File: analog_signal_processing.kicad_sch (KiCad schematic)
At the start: 62 parts, among them U3 PT2399, U4 CD4066BE, U5 PT2399, U8 TL072, U9 TL072

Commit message: wip on esp conns
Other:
- moved on the sheet: C34, C35, R26, R29, U4C
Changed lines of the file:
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@@
 	(wire
 		(pts
+			(xy 63.5 172.72) (xy 63.5 165.1)
+		)
+		(stroke
+			(width 0)
+			(type default)
+		)
+	)
+	(wire
+		(pts
 			(xy 243.84 35.56) (xy 247.65 35.56)
 		)
@@
 	(wire
 		(pts
+			(xy 60.96 135.89) (xy 90.17 135.89)
+		)
+		(stroke
+			(width 0)
+			(type default)
+		)
+	)
+	(wire
+		(pts
 			(xy 198.12 54.61) (xy 198.12 55.88)
 		)
@@
 	(wire
 		(pts
-			(xy 67.31 128.27) (xy 67.31 130.81)
+			(xy 38.1 128.27) (xy 38.1 130.81)
 		)
 		(stroke
@@
 	(wire
 		(pts
-			(xy 95.25 146.05) (xy 95.25 147.32)
+			(xy 48.26 172.72) (xy 63.5 172.72)
 		)
 		(stroke
@@
 	(wire
 		(pts
-			(xy 198.12 16.51) (xy 198.12 19.05)
+			(xy 95.25 146.05) (xy 95.25 147.32)
 		)
 		(stroke
@@
 	(wire
 		(pts
-			(xy 138.43 83.82) (xy 138.43 85.09)
+			(xy 198.12 16.51) (xy 198.12 19.05)
 		)
 		(stroke
@@
 	(wire
 		(pts
-			(xy 154.94 31.75) (xy 160.02 31.75)
+			(xy 138.43 83.82) (xy 138.43 85.09)
 		)
 		(stroke
@@
 	(wire
 		(pts
-			(xy 107.95 33.02) (xy 107.95 41.91)
+			(xy 154.94 31.75) (xy 160.02 31.75)
 		)
 		(stroke
@@
 	(wire
 		(pts
-			(xy 63.5 165.1) (xy 63.5 172.72)
+			(xy 107.95 33.02) (xy 107.95 41.91)
 		)
 		(stroke
@@
 	(global_label "AUDIO_IN"
 		(shape input)
-		(at 59.69 135.89 180)
+		(at 30.48 135.89 180)
 		(fields_autoplaced yes)
 		(effects
@@
 		)
 		(property "Intersheetrefs" "${INTERSHEET_REFS}"
-			(at 48.1775 135.89 0)
+			(at 18.9675 135.89 0)
 			(effects
 				(font
@@
 	(global_label "U4C"
 		(shape input)
-		(at 67.31 128.27 0)
+		(at 38.1 128.27 0)
 		(fields_autoplaced yes)
 		(effects
@@
 		)
 		(property "Intersheetrefs" "${INTERSHEET_REFS}"
-			(at 74.1052 128.27 0)
+			(at 44.8952 128.27 0)
 			(effects
 				(font
@@
 	(global_label "Output_Tap"
 		(shape input)
-		(at 48.26 172.72 180)
+		(at 33.02 172.72 180)
 		(fields_autoplaced yes)
 		(effects
@@
 		)
 		(property "Intersheetrefs" "${INTERSHEET_REFS}"
-			(at 34.8127 172.72 0)
+			(at 19.5727 172.72 0)
 			(effects
 				(font
@@
 	(symbol
 		(lib_id "PCM_4ms_Resistor:4.7k_0603")
-		(at 86.36 135.89 90)
+		(at 57.15 135.89 90)
 		(unit 1)
 		(exclude_from_sim no)
@@
 		(dnp no)
 		(property "Reference" "R29"
-			(at 86.36 131.826 90)
+			(at 57.15 131.826 90)
 			(effects
 				(font
@@
 		)
 		(property "Value" "4.7k_0603"
-			(at 86.36 138.43 90)
+			(at 57.15 138.43 90)
 			(effects
 				(font
@@
 		)
 		(property "Footprint" "4ms_Resistor:R_0603"
-			(at 99.06 138.43 0)
+			(at 69.85 138.43 0)
 			(effects
 				(font
@@
 		)
 		(property "Datasheet" ""
-			(at 86.36 135.89 0)
+			(at 57.15 135.89 0)
 			(effects
 				(font
@@
 		)
 		(property "Description" "4k7, 1%, 1/10W, 0603"
-			(at 86.36 135.89 0)
+			(at 57.15 135.89 0)
 			(effects
 				(font
@@
 		)
 		(property "Specifications" "4k7, 1%, 1/10W, 0603"
-			(at 94.234 138.43 0)
+			(at 65.024 138.43 0)
 			(effects
 				(font
@@
 		)
 		(property "Manufacturer" "Yageo"
-			(at 95.758 138.43 0)
+			(at 66.548 138.43 0)
 			(effects
 				(font
@@
 		)
 		(property "Part Number" "RC0603FR-074K7L"
-			(at 97.282 138.43 0)
+			(at 68.072 138.43 0)
 			(effects
 				(font
@@
 		)
 		(property "Display" "4.7k"
-			(at 86.36 133.604 90)
+			(at 57.15 133.604 90)
 			(effects
 				(font
@@
 		)
 		(property "JLCPCB ID" "C23162"
-			(at 86.36 135.89 0)
+			(at 57.15 135.89 0)
 			(effects
 				(font
@@
 	(symbol
 		(lib_id "Device:C_Polarized")
-		(at 59.69 172.72 90)
+		(at 44.45 172.72 90)
 		(unit 1)
 		(exclude_from_sim no)
@@
 		(dnp no)
 		(property "Reference" "C35"
-			(at 59.69 166.878 90)
+			(at 44.45 166.878 90)
 			(effects
 				(font
@@
 		)
 		(property "Value" "47 uF"
-			(at 59.69 168.656 90)
+			(at 44.45 168.656 90)
 			(effects
 				(font
@@
 		)
 		(property "Footprint" ""
-			(at 63.5 171.7548 0)
+			(at 48.26 171.7548 0)
 			(effects
 				(font
@@
 		)
 		(property "Datasheet" "~"
-			(at 59.69 172.72 0)
+			(at 44.45 172.72 0)
 			(effects
 				(font
@@
 		)
 		(property "Description" "Polarized capacitor"
-			(at 59.69 172.72 0)
+			(at 44.45 172.72 0)
 			(effects
 				(font
@@
 		(on_board yes)
 		(dnp no)
-		(fields_autoplaced yes)
 		(property "Reference" "POT2"
-			(at 68.58 167.6399 0)
+			(at 69.342 167.64 0)
 			(effects
 				(font
@@
 		)
 		(property "Display" "10k"
-			(at 68.58 170.1799 0)
+			(at 69.342 170.18 0)
 			(effects
 				(font
@@
 	(symbol
 		(lib_id "PCM_4ms_Resistor:4.7k_0603")
-		(at 52.07 172.72 90)
+		(at 36.83 172.72 90)
 		(unit 1)
 		(exclude_from_sim no)
@@
 		(dnp no)
 		(property "Reference" "R26"
-			(at 52.07 168.656 90)
+			(at 36.83 168.656 90)
 			(effects
 				(font
@@
 		)
 		(property "Value" "4.7k_0603"
-			(at 52.07 175.26 90)
+			(at 36.83 175.26 90)
 			(effects
 				(font
@@
 		)
 		(property "Footprint" "4ms_Resistor:R_0603"
-			(at 64.77 175.26 0)
+			(at 49.53 175.26 0)
 			(effects
 				(font
@@
 		)
 		(property "Datasheet" ""
-			(at 52.07 172.72 0)
+			(at 36.83 172.72 0)
 			(effects
 				(font
@@
 		)
 		(property "Description" "4k7, 1%, 1/10W, 0603"
-			(at 52.07 172.72 0)
+			(at 36.83 172.72 0)
 			(effects
 				(font
@@
 		)
 		(property "Specifications" "4k7, 1%, 1/10W, 0603"
-			(at 59.944 175.26 0)
+			(at 44.704 175.26 0)
 			(effects
 				(font
@@
 		)
 		(property "Manufacturer" "Yageo"
-			(at 61.468 175.26 0)
+			(at 46.228 175.26 0)
 			(effects
 				(font
@@
 		)
 		(property "Part Number" "RC0603FR-074K7L"
-			(at 62.992 175.26 0)
+			(at 47.752 175.26 0)
 			(effects
 				(font
@@
 		)
 		(property "Display" "4.7k"
-			(at 52.07 170.434 90)
+			(at 36.83 170.434 90)
 			(effects
 				(font
@@
 		)
 		(property "JLCPCB ID" "C23162"
-			(at 52.07 172.72 0)
+			(at 36.83 172.72 0)
 			(effects
 				(font
@@
 	(symbol
 		(lib_id "Analog_Switch:CD4066BE")
-		(at 67.31 135.89 180)
+		(at 38.1 135.89 180)
 		(unit 3)
 		(exclude_from_sim no)
@@
 		(fields_autoplaced yes)
 		(property "Reference" "U4"
-			(at 67.31 140.97 0)
+			(at 38.1 140.97 0)
 			(effects
 				(font
@@
 		)
 		(property "Value" "CD4066BE"
-			(at 67.31 143.51 0)
+			(at 38.1 143.51 0)
 			(effects
 				(font
@@
 		)
 		(property "Footprint" "Package_DIP:DIP-14_W7.62mm"
-			(at 67.31 133.35 0)
+			(at 38.1 133.35 0)
 			(effects
 				(font
@@
 		)
 		(property "Datasheet" "https://www.ti.com/lit/ds/symlink/cd4066b.pdf"
-			(at 67.31 135.89 0)
+			(at 38.1 135.89 0)
 			(effects
 				(font
@@
 		)
 		(property "Description" "Quad 20V analog SPST 1:1 switch, DIP-14"
-			(at 67.31 135.89 0)
+			(at 38.1 135.89 0)
 			(effects
 				(font
@@
 	(symbol
 		(lib_id "Device:C_Polarized")
-		(at 78.74 135.89 90)
+		(at 49.53 135.89 90)
 		(unit 1)
 		(exclude_from_sim no)
@@
 		(dnp no)
 		(property "Reference" "C34"
-			(at 78.74 130.048 90)
+			(at 49.53 130.048 90)
 			(effects
 				(font
@@
 		)
 		(property "Value" "47 uF"
-			(at 78.74 131.826 90)
+			(at 49.53 131.826 90)
 			(effects
 				(font
@@
 		)
 		(property "Footprint" ""
-			(at 82.55 134.9248 0)
+			(at 53.34 134.9248 0)
 			(effects
 				(font
@@
 		)
 		(property "Datasheet" "~"
-			(at 78.74 135.89 0)
+			(at 49.53 135.89 0)
 			(effects
 				(font
@@
 		)
 		(property "Description" "Polarized capacitor"
-			(at 78.74 135.89 0)
+			(at 49.53 135.89 0)
 			(effects
 				(font

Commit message: fixed a lot of things
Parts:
- removed C10, C11, C18, C19, C23, C34, C35, C36, C37, C39, C4, C5, C6: 47 uF, symbol Device:C_Polarized
- removed C12, C22, C24, C9: 3.3nF, symbol Device:C
- removed C13, C20, C25, C7: 6.8 nF, symbol Device:C
- removed C14, C15, C16, C17, C21, C26, C27, C28, C29, C8: 100nF, symbol Device:C
- removed C2, C33, C38: 100nF_0603_16V, 4ms_Capacitor:C_0603, symbol PCM_4ms_Capacitor:100nF_0603_16V
- removed R1: 1M, symbol Device:R
- removed R10, R11, R12, R13, R14, R15, R16, R17, R18, R19, R26, R27, R28, R29, R30, R7, R8, R9: 4.7k_0603, 4ms_Resistor:R_0603, symbol PCM_4ms_Resistor:4.7k_0603
- removed R6: 5k, symbol Device:R
- removed U8: TL072, 4ms_Package_SSOP:TSSOP-8_4.4x3mm_Pitch0.65mm, symbol PCM_4ms_IC:TL072
- removed unit 1 of U9
- added AUX_OUT1: NJ2FD-V, Connector_Audio:Jack_6.35mm_Neutrik_NJ2FD-V_Vertical, symbol Connector_Audio:NJ2FD-V
- added C10, C11, C18, C19, C2, C23, C31, C32, C34, C36, C41, C5, C6: 47uF, CAPPRD200W50D525H1250, symbol SamacSys_Parts:REA470M1CBK-0511P
- added C12, C14, C15, C16, C17, C21, C26, C27, C28, C3, C30, C37, C8: 100nF, SR211C104KARTR1, symbol SamacSys_Parts:SR211C104KARTR1
- added C13, C25, C38, C7: 6.8nF, SR211C682MARTR1, symbol SamacSys_Parts:SR211C682MARTR1
- added C20, C22, C24, C9: 3.3nF, RCER72A332K0DBH03A, symbol SamacSys_Parts:RCER72A332K0DBH03A
- added IC1: TL072CP, DIP794W53P254L959H508Q8N, symbol SamacSys_Parts:TL072CP
- added R1: 5k, RESAD1550W60L630D230, symbol SamacSys_Parts:YR1B4K99CC
- added R10, R11, R12, R13, R14, R15, R16, R17, R18, R19, R22, R23, R24, R25, R26, R7, R8, R9: 4.7k, RESAD1590W60L630D240, symbol SamacSys_Parts:MFR-25FRF52-4K7
- added R27: 1M, RESAD1590W60L630D240, symbol SamacSys_Parts:MFR-25FRF52-1M
- added U2: TL072, 4ms_Package_SSOP:TSSOP-8_4.4x3mm_Pitch0.65mm, symbol PCM_4ms_IC:TL072
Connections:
- net +5V: now also C12.1, C28.2, C30.2, U2.5 (+)
- net +9V: now also C37.1, U2.8 (V+)
- net AUDIO_IN: now also R22.1, U2.1, U2.2 (-)
- net EFFECT_OUT: now also AUX_OUT1.T, C23.2
- net MIDDLE_TAP: now also C6.2
- net OUTPUT_TAP: now also C20.1, R16.1
- net Output_Tap: now also C41.2, R24.1
- net at U3.15 (LPF1-OUT): now also C24.2, R8.1
- net at U5.10 (OP1-IN): now also C26.1
- net at U5.11 (OP2-IN): now also C17.2
- net at U5.12 (OP2-OUT): now also C17.1, R18.1
- net at U5.13 (LPF2-IN): now also C20.2, R17.1
- net at U5.15 (LPF1-OUT): now also C9.2, R15.1
- net at U5.16 (LPF1-IN): now also C9.1, R14.1
- net at U5.2 (REF): now also C19.1
- net at U5.7 (CC1): now also C21.2
- net at U5.8 (CC0): now also C27.2
- net at U5.9 (OP1-OUT): now also C26.2
- net at U3.16 (LPF1-IN): now also C24.1, R7.1
- net at U3.14 (LPF2-OUT): now also C22.1, C6.1, R9.1
- net Effect In: now reaches AUX_IN1.T
- net Effect In: now also C3.2
- net at POT2.1 (Left): now also C32.2, C36.2
- net at U4.1: now also R23.1
- net at U4.4: now also R12.2
- net at POT1.1 (Left): now also C41.1
- net at POT1.2 (Center): now also R1.1
- net at U4.11: now also R13.2
- net at POT2.2 (Center): now also C34.1
- net at U3.13 (LPF2-IN): now also C22.2, R10.1
- net at U3.12 (OP2-OUT): now also C14.1, R11.1
- net at U3.11 (OP2-IN): now also C14.2
- net at U4.8: now also C31.1
- net at U3.10 (OP1-IN): now also C16.1
- net at U3.9 (OP1-OUT): now also C16.2
- net at U3.7 (CC1): now also C8.2
- net at U3.8 (CC0): now also C15.2
- net at U3.2 (REF): now also C2.1
- net GNDA renamed GND
- net GND: now also AUX_OUT1.S, C12.2, C13.1, C15.1, C19.2, C2.2, C21.1, C25.2, C27.1, C28.1, C30.1, C37.2, C38.2, C7.1, C8.1, U2.4 (V-)
- new net: C36.1, R24.2
- new net: C34.2, R25.1
- new net: C3.1, R27.2, U2.3 (+)
- new net: C10.1, R22.2
- new net: R19.2, R25.2, R26.1, U2.6 (-)
- new net: C23.1, R26.2, U2.7
- new net: C18.1, R12.1
- new net: C31.2, R19.1
- new net: C10.2, C13.2, C5.2, R7.2, R8.2
- new net: C11.2, C18.2, C7.2, R14.2, R15.2
- new net: C25.1, R16.2, R17.2, R18.2
- new net: C38.1, R10.2, R11.2, R9.2
- new net: C11.1, R13.1
- new net: C5.1, R1.2
- new net: C32.1, R23.2
- new net 4.5V: R27.1
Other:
- note added: "Output Connector"

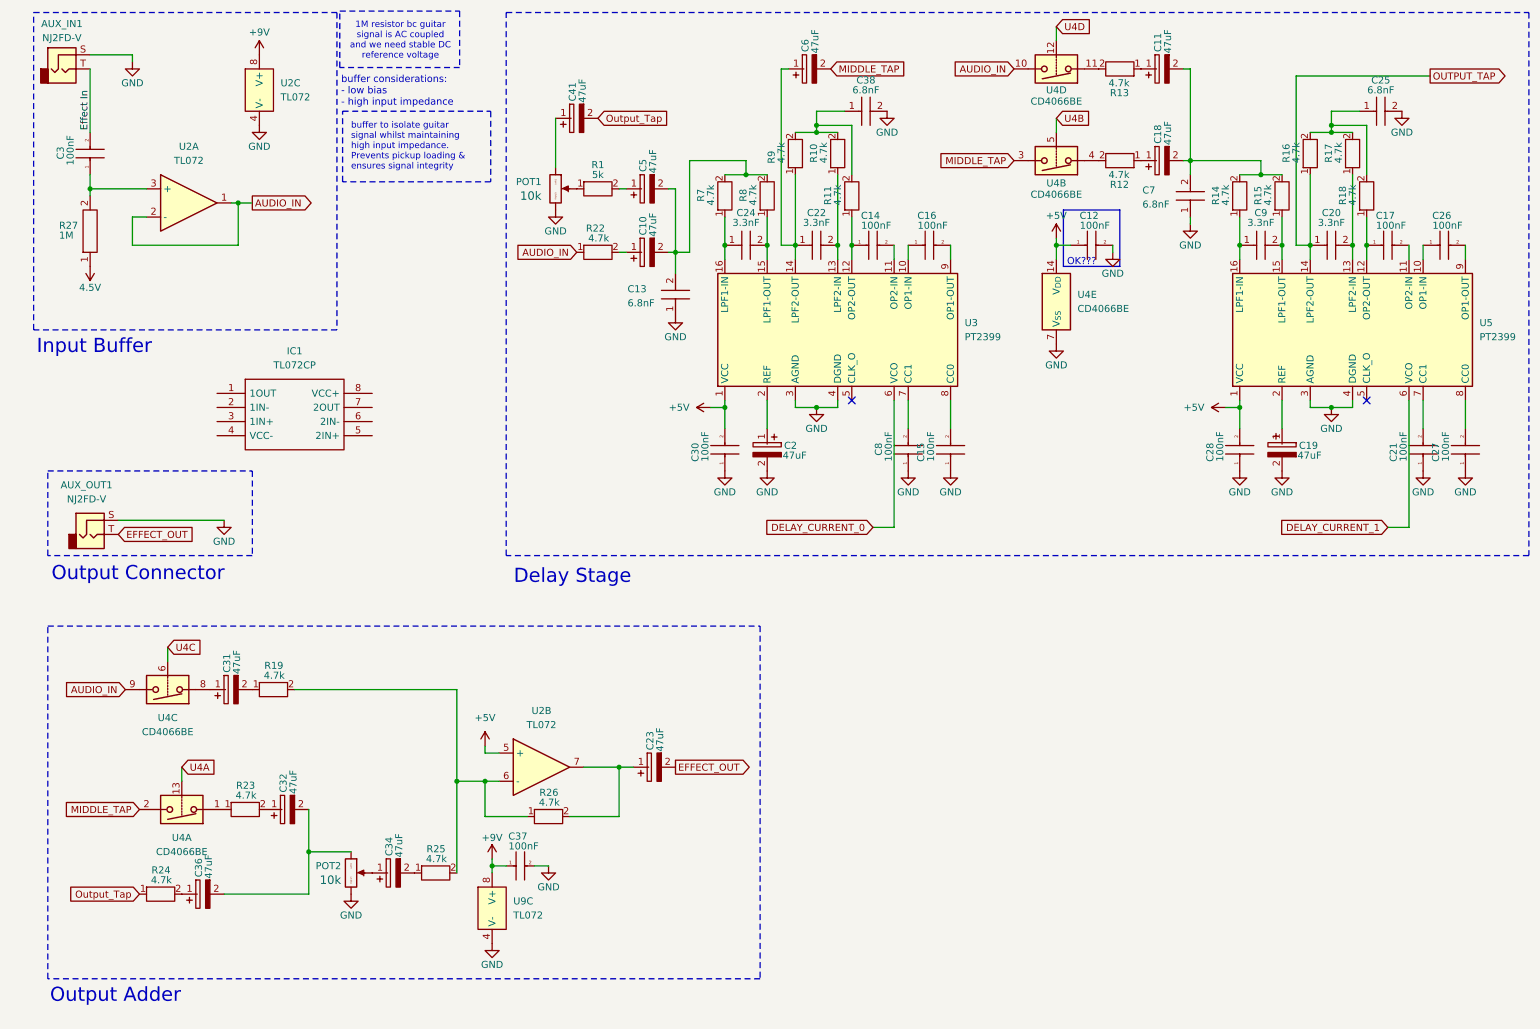
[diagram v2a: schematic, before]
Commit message: initial board routing
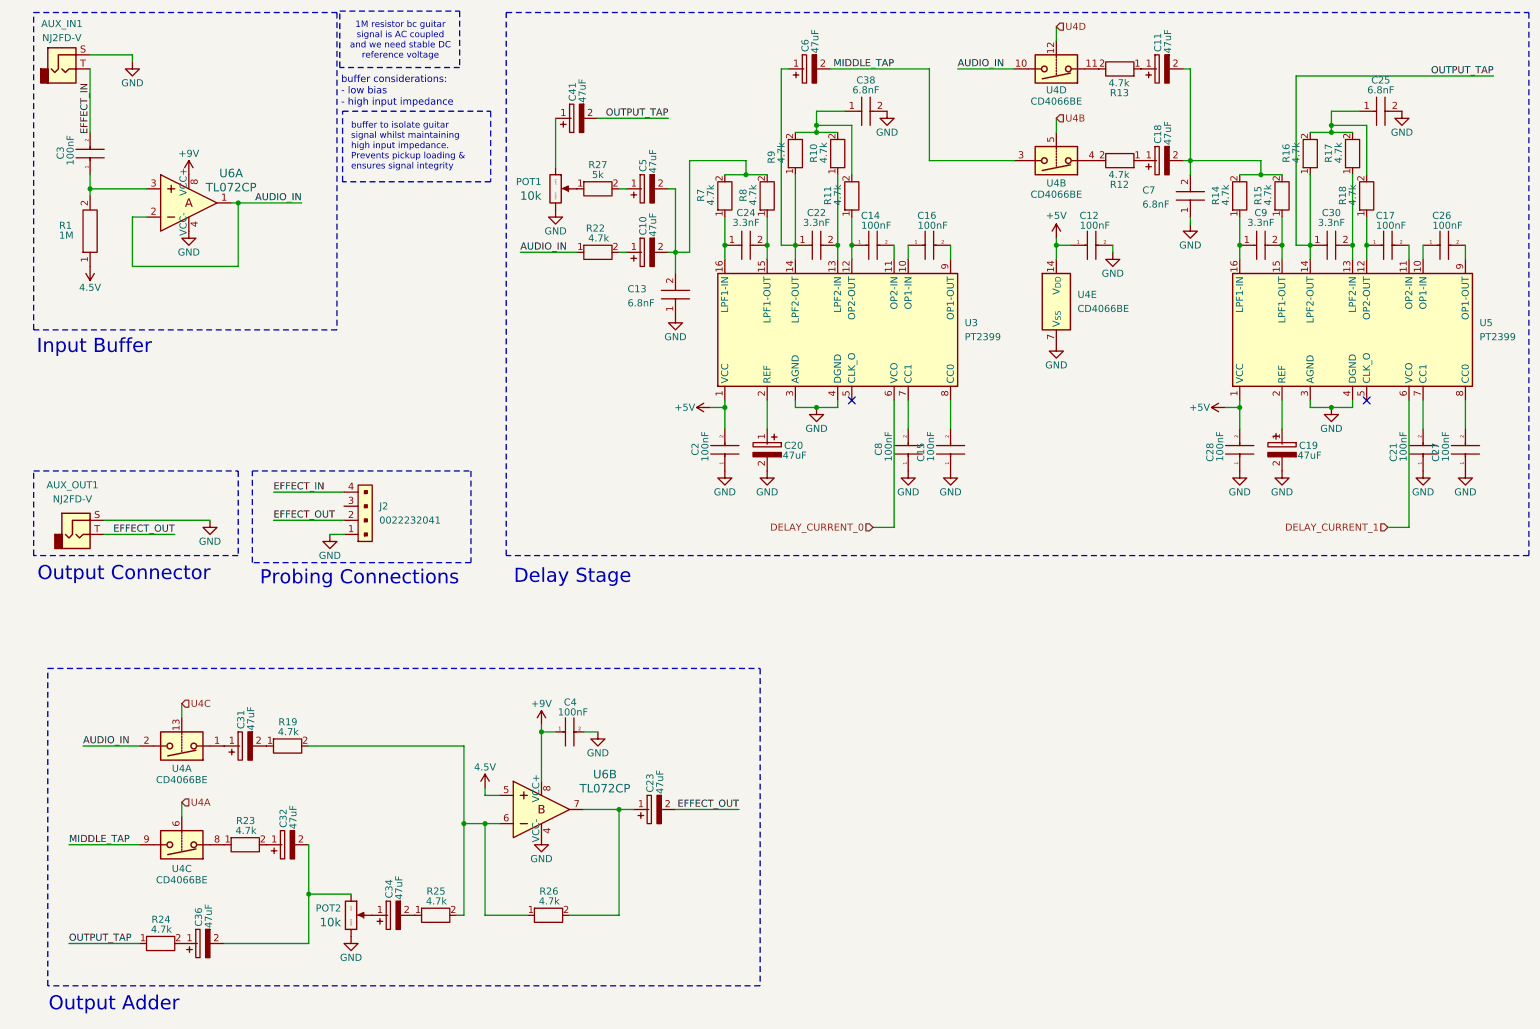
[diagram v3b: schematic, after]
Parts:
- removed C37: 100nF, SR211C104KARTR1, symbol SamacSys_Parts:SR211C104KARTR1
- removed IC1: TL072CP, DIP794W53P254L959H508Q8N, symbol SamacSys_Parts:TL072CP
- removed U2, U9: TL072, 4ms_Package_SSOP:TSSOP-8_4.4x3mm_Pitch0.65mm, symbol PCM_4ms_IC:TL072
- removed unit 1 of U4
- added C4: 100nF, digikey-footprints:1206, symbol SamacSys_Parts:SR211C104KARTR1
- added J2: 0022232041, digikey-footprints:PinHeader_1x4_P2.54mm_Drill1.02mm, symbol dk_Rectangular-Connectors-Headers-Male-Pins:0022232041
- added unit 3 of U4
- added U6: TL072CP, digikey-footprints:DIP-8_W7.62mm, symbol dk_Linear-Amplifiers-Instrumentation-OP-Amps-Buffer-Amps:TL072CP
- C10, C11, C18, C19, C23, C31, C32, C34, C36, C41, C5, C6: footprint CAPPRD200W50D525H1250 -> digikey-footprints:1206
- C12, C14, C15, C16, C17, C21, C26, C27, C28, C3, C8: footprint SR211C104KARTR1 -> digikey-footprints:1206
- C13, C25, C38, C7: footprint SR211C682MARTR1 -> digikey-footprints:1206
- C2: renamed from C30; footprint SR211C104KARTR1 -> digikey-footprints:1206
- C20: renamed from C2; footprint CAPPRD200W50D525H1250 -> digikey-footprints:1206
- C22, C24, C9: footprint RCER72A332K0DBH03A -> digikey-footprints:1206
- C30: renamed from C20; footprint RCER72A332K0DBH03A -> digikey-footprints:1206
- POT1, POT2: footprint 4ms_Potentiometer:Pot_16mm_NoDet_RV16AF-4A -> Potentiometer_THT:KRISTOF_POT
- R1: renamed from R27; footprint RESAD1590W60L630D240 -> digikey-footprints:1206
- R10, R11, R12, R13, R14, R15, R16, R17, R18, R19, R22, R23, R24, R25, R26, R7, R8, R9: footprint RESAD1590W60L630D240 -> digikey-footprints:1206
- R27: renamed from R1; footprint RESAD1550W60L630D230 -> digikey-footprints:1206
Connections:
- net Output_Tap is gone; now on net OUTPUT_TAP: C41.2, R24.1
- net +9V: now also C4.1, U6.8 (VCC+), U6.8 (VCC+)
- net 4.5V: now also U6.5
- net AUDIO_IN: now also U4.2, U6.1, U6.2; no longer U4.9
- net EFFECT_OUT: now also J2.2
- net GND: now also C4.2, J2.1, U6.4 (VCC-), U6.4 (VCC-)
- net MIDDLE_TAP: now also U4.9
- net U4A: now also U4.6
- net U4C: now also U4.13; no longer U4.6
- net at C3.1, R1.2: now also U6.3
- net at R19.2, R25.2, R26.1: now also U6.6
- net at C23.1, R26.2: now also U6.7
- net at R23.1: now also U4.8
- net at C31.1: now also U4.1; no longer U4.8
- net Effect In renamed EFFECT_IN
- net EFFECT_IN: now also J2.4
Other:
- note added: "Probing Connections"
- note removed: "OK???"
- moved on the sheet: AUX_OUT1, C23, C31, C32, C34, C36, POT2, R19, R23, R24, R25, R26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
